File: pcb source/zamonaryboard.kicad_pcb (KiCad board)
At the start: 2 copper layers, 52.3 x 40.6 mm, 19 parts, among them J1 USB_C_Receptacle_USB2.0_14P, SW1 SW_Push, U1 ESP32-S2, U2 ME6211C33M5, Y1 Crystal_GND24

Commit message: Added jlcpcb component annotations, small improvements
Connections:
- U1 pad 30: unconnected-(U1-VDD_SPI-Pad30) -> +3V3
- U1 pad 48: unconnected-(U1-U0TXD/GPIO43-Pad48) -> TX
- U1 pad 49: unconnected-(U1-U0RXD/GPIO44-Pad49) -> RX
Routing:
- net RX: track 0.00 -> 6.73 mm
- net TX: track 0.00 -> 5.18 mm
- net +3V3: track 53.1 -> 57.0 mm, vias 5 -> 6
- net Net-(U1-XTAL_N): track 12.3 -> 13.1 mm
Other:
- board text added: "RX"
- board text added: "TX"
- board text added: "prototype 1.2.1"
- board text removed: "prototype 1.1"

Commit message: big improvements to pcb
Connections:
- C1 pad 1: Net-(C1-Pad1) -> +3V3
- C2 pad 1: Net-(C1-Pad1) -> +3V3
- C3 pad 1: Net-(C1-Pad1) -> +3V3
- U1 pad 3: Net-(C1-Pad1) -> +3V3
- U1 pad 4: Net-(C1-Pad1) -> +3V3
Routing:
- net Net-(C1-Pad1): track 16.4 -> 0.00 mm, vias 2 -> 0
- net +3V3: track 57.0 -> 66.6 mm
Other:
- board text added: "prototype 1.3"
- board text removed: "prototype 1.2.1"

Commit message: exported gerber files for prototype 1.3, cleanup
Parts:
- C8, C9: footprint Capacitor_SMD:C_0805_2012Metric_Pad1.18x1.45mm_HandSolder -> Capacitor_SMD:C_0603_1608Metric_Pad1.08x0.95mm_HandSolder
- Y1: footprint Crystal:Crystal_SMD_3225-4Pin_3.2x2.5mm_HandSoldering -> Crystal:Crystal_SMD_3225-4Pin_3.2x2.5mm
- moved C8 1.04 mm to (153.1, 78.4)
- moved Y1 0.69 mm to (150.3, 78.5)
- moved C9 0.36 mm to (150.3, 75.4)
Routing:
- net GND: track 119.8 -> 105.5 mm
- net Net-(U1-XTAL_N): track 13.1 -> 9.63 mm
- net Net-(U1-XTAL_P): track 6.39 -> 5.77 mm

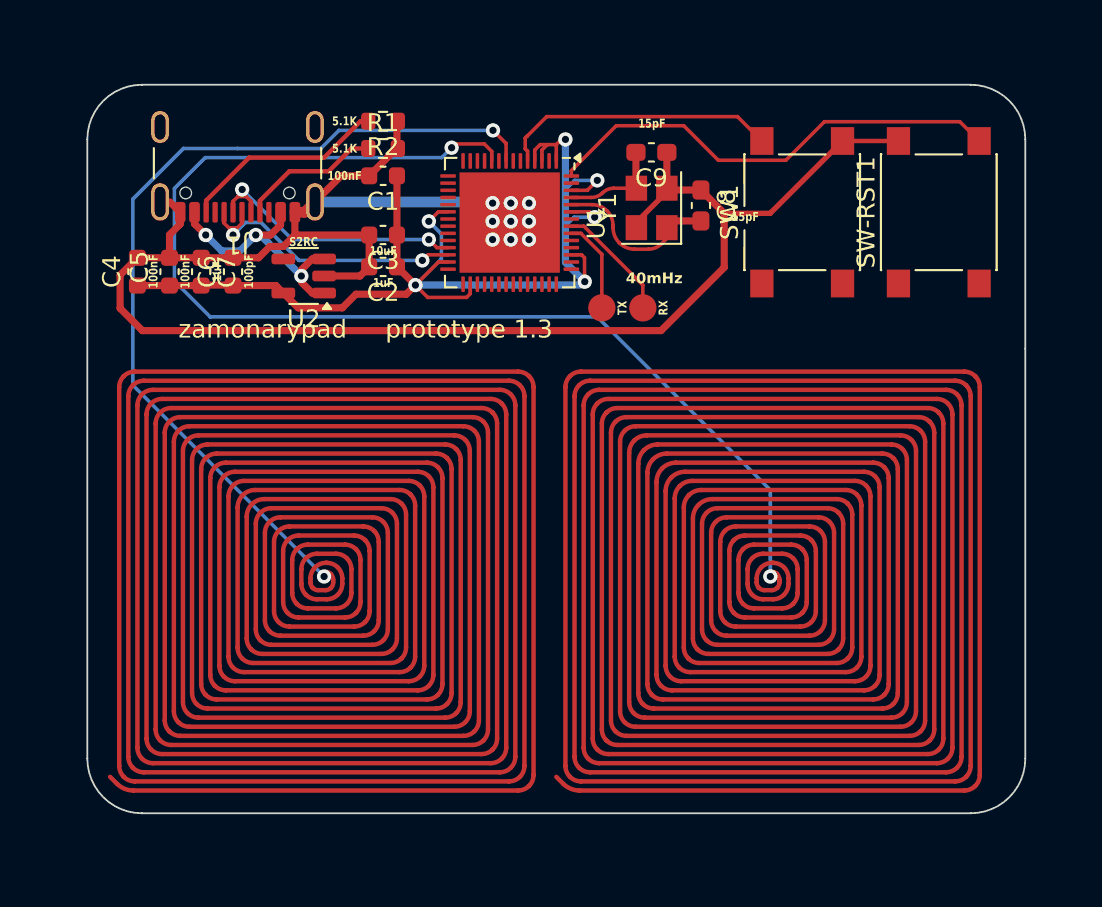
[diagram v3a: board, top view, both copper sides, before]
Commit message: Many improvements to pcb and scheme, added testpoints for easier debugging
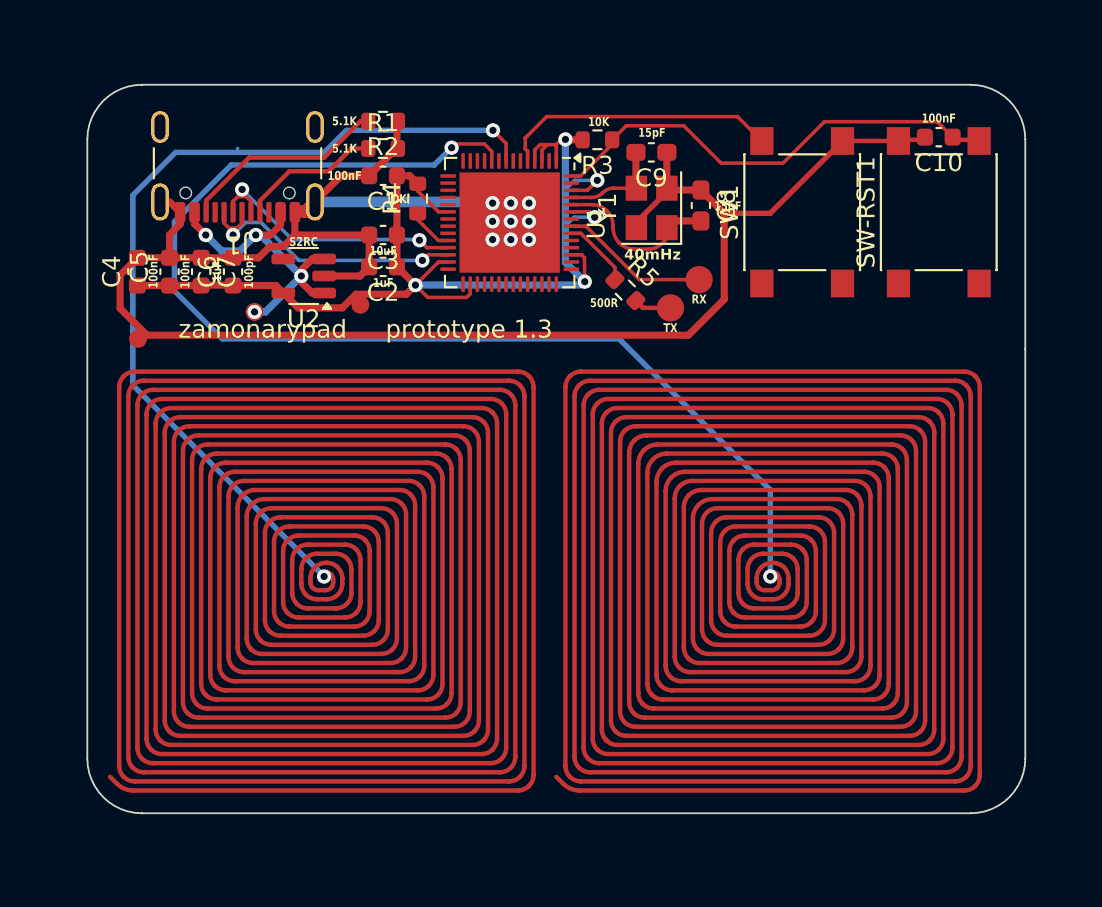
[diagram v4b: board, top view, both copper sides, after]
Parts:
- added C10: 100nF, Capacitor_SMD:C_0603_1608Metric, F.Cu at (166.4, 74.6)
- added R3: 10K, Resistor_SMD:R_0603_1608Metric, F.Cu at (147.3, 74.7)
- added R4: 10K, Resistor_SMD:R_0603_1608Metric, F.Cu at (137.3, 78.0)
- added R5: 500, Resistor_SMD:R_0603_1608Metric, F.Cu at (148.9, 83.1)
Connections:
- U1 pad 24: unconnected-(U1-GPIO18/ADC2_CH7/DAC_2-Pad24) -> Net-(U1-GPIO18/ADC2_CH7/DAC_2)
- U1 pad 48: TX -> Net-(U1-U0TXD/GPIO43)
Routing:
- net Net-(U1-U0TXD/GPIO43): track 0.00 -> 3.90 mm
- net VBUS: track 14.6 -> 18.0 mm, vias 3 -> 4
- net TX: track 5.18 -> 2.10 mm
- net Net-(U1-GPIO18/ADC2_CH7/DAC_2): track 0.00 -> 2.53 mm
- net GND: track 105.5 -> 107.9 mm
- net RX: track 6.62 -> 8.37 mm
- net +3V3: track 66.6 -> 65.6 mm, vias 6 -> 5
- net BTN2: track 1143.1 -> 1142.3 mm
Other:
- board text added: "10K"
- board text added: "500R"

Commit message: improved routing, fixes
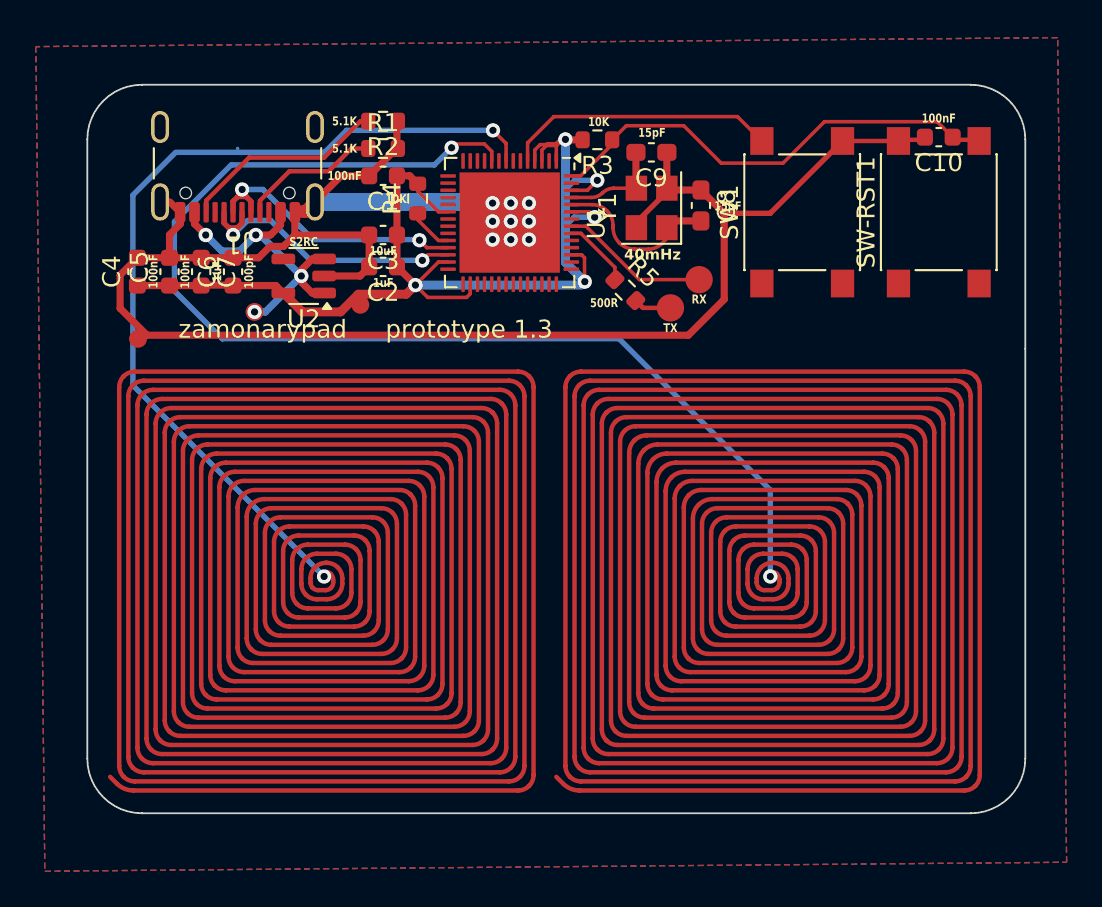
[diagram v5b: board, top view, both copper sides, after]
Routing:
- added copper zone on B.Cu, net (none)
- added copper zone on F.Cu, net (none)
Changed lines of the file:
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@@
 	)
 	(setup
+		(stackup
+			(layer "F.SilkS"
+				(type "Top Silk Screen")
+			)
+			(layer "F.Paste"
+				(type "Top Solder Paste")
+			)
+			(layer "F.Mask"
+				(type "Top Solder Mask")
+				(thickness 0.01)
+			)
+			(layer "F.Cu"
+				(type "copper")
+				(thickness 0.035)
+			)
+			(layer "dielectric 1"
+				(type "core")
+				(thickness 1.51)
+				(material "FR4")
+				(epsilon_r 4.5)
+				(loss_tangent 0.02)
+			)
+			(layer "B.Cu"
+				(type "copper")
+				(thickness 0.035)
+			)
+			(layer "B.Mask"
+				(type "Bottom Solder Mask")
+				(thickness 0.01)
+			)
+			(layer "B.Paste"
+				(type "Bottom Solder Paste")
+			)
+			(layer "B.SilkS"
+				(type "Bottom Silk Screen")
+			)
+			(copper_finish "None")
+			(dielectric_constraints no)
+		)
 		(pad_to_mask_clearance 0)
 		(allow_soldermask_bridges_in_footprints no)
@@
 	)
 	(segment
-		(start 141.411 78.165)
-		(end 141.478 78.232)
-		(width 0.25)
+		(start 142.5 79.25)
+		(end 142.496 79.25)
+		(width 1)
 		(layer "B.Cu")
 		(net 1)
@@
 	(segment
 		(start 131.57 78.165)
-		(end 141.411 78.165)
-		(width 0.6)
+		(end 141.415 78.165)
+		(width 1)
 		(layer "B.Cu")
 		(net 1)
 	)
 	(segment
-		(start 133.858 83.312)
-		(end 136.66464 83.312)
-		(width 0.4)
-		(layer "F.Cu")
-		(net 2)
+		(start 142.496 79.25)
+		(end 142.494 79.248)
+		(width 1)
+		(layer "B.Cu")
+		(net 1)
 	)
 	(segment
@@
 	)
 	(segment
-		(start 133.096 84.074)
-		(end 133.858 83.312)
-		(width 0.4)
+		(start 129.805 83.246)
+		(end 130.859 84.3)
+		(width 0.5)
 		(layer "F.Cu")
 		(net 2)
@@
 		(start 145.032 74.968)
 		(end 144.532 74.968)
-		(width 0.2)
+		(width 0.3)
+		(layer "F.Cu")
+		(net 2)
+	)
+	(segment
+		(start 136.66464 83.312)
+		(end 137.17264 82.804)
+		(width 0.5)
 		(layer "F.Cu")
 		(net 2)
@@
 	)
 	(segment
+		(start 130.859 84.3)
+		(end 133 84.3)
+		(width 0.5)
+		(layer "F.Cu")
+		(net 2)
+	)
+	(segment
 		(start 146.766 77.516)
 		(end 145.8695 77.516)
@@
 	)
 	(segment
-		(start 145.324 74.676)
-		(end 145.032 74.968)
-		(width 0.2)
+		(start 133.988 83.312)
+		(end 136.66464 83.312)
+		(width 0.5)
 		(layer "F.Cu")
 		(net 2)
 	)
 	(segment
-		(start 130.633 84.074)
-		(end 133.096 84.074)
-		(width 0.4)
+		(start 145.324 74.676)
+		(end 145.032 74.968)
+		(width 0.3)
 		(layer "F.Cu")
 		(net 2)
@@
 	)
 	(segment
-		(start 129.805 83.246)
-		(end 130.633 84.074)
-		(width 0.4)
-		(layer "F.Cu")
-		(net 2)
-	)
-	(segment
 		(start 125.248 82.804)
 		(end 125.222 82.83)
@@
 	)
 	(segment
-		(start 136.66464 83.312)
-		(end 137.17264 82.804)
-		(width 0.4)
-		(layer "F.Cu")
-		(net 2)
-	)
-	(segment
 		(start 144.232 75.268)
 		(end 144.232 75.8785)
@@
 	)
 	(segment
+		(start 133 84.3)
+		(end 133.988 83.312)
+		(width 0.5)
+		(layer "F.Cu")
+		(net 2)
+	)
+	(segment
 		(start 129.389 82.83)
 		(end 129.805 83.246)
@@
 		(start 147.174275 79.016)
 		(end 146.028 79.016)
-		(width 0.2)
+		(width 0.3)
 		(layer "B.Cu")
 		(net 2)
@@
 		(start 146.05 76.962)
 		(end 145.542 77.47)
-		(width 0.2)
+		(width 0.3)
 		(layer "B.Cu")
 		(net 2)
@@
 		(start 146.431 82.804)
 		(end 137.17264 82.804)
-		(width 0.4)
+		(width 0.5)
 		(layer "B.Cu")
 		(net 2)
@@
 		(start 147.32 76.962)
 		(end 146.05 76.962)
-		(width 0.2)
+		(width 0.3)
 		(layer "B.Cu")
 		(net 2)
@@
 		(start 146.6215 82.6135)
 		(end 145.542 81.534)
-		(width 0.4)
+		(width 0.5)
 		(layer "B.Cu")
 		(net 2)
@@
 		(start 145.542 81.534)
 		(end 145.542 79.756)
-		(width 0.4)
+		(width 0.5)
 		(layer "B.Cu")
 		(net 2)
@@
 		(start 145.542 79.756)
 		(end 145.542 77.47)
-		(width 0.4)
+		(width 0.5)
 		(layer "B.Cu")
 		(net 2)
@@
 		(start 145.542 74.676)
 		(end 145.542 77.47)
-		(width 0.4)
+		(width 0.5)
 		(layer "B.Cu")
 		(net 2)
@@
 		(start 146.028 79.016)
 		(end 145.542 79.502)
-		(width 0.2)
+		(width 0.3)
 		(layer "B.Cu")
 		(net 2)
@@
 		(start 126.5 79.34741)
 		(end 126.5 78.74)
-		(width 0.2)
+		(width 0.3)
 		(layer "F.Cu")
 		(net 3)
@@
 		(start 127.23241 79.615)
 		(end 126.76759 79.615)
-		(width 0.2)
+		(width 0.3)
 		(layer "F.Cu")
 		(net 3)
@@
 		(start 126.76759 79.615)
 		(end 126.5 79.34741)
-		(width 0.2)
+		(width 0.3)
 		(layer "F.Cu")
 		(net 3)
@@
 		(start 127.5 79.34741)
 		(end 127.23241 79.615)
-		(width 0.2)
+		(width 0.3)
 		(layer "F.Cu")
 		(net 3)
@@
 		(start 127.5 78.74)
 		(end 127.5 79.34741)
-		(width 0.2)
+		(width 0.3)
 		(layer "F.Cu")
 		(net 3)
@@
 	)
 	(segment
-		(start 127.7 79.31)
-		(end 127 80.01)
-		(width 0.2)
+		(start 129.1 79.2)
+		(end 127.81 79.2)
+		(width 0.3)
 		(layer "B.Cu")
 		(net 3)
 	)
 	(segment
-		(start 137.560345 81.426345)
-		(end 130.676295 81.426345)
-		(width 0.2)
+		(start 131.326345 81.426345)
+		(end 129.1 79.2)
+		(width 0.3)
 		(layer "B.Cu")
 		(net 3)
 	)
 	(segment
-		(start 128.55995 79.31)
-		(end 127.7 79.31)
-		(width 0.2)
+		(start 127.81 79.2)
+		(end 127 80.01)
+		(width 0.3)
 		(layer "B.Cu")
 		(net 3)
 	)
 	(segment
-		(start 130.676295 81.426345)
-		(end 128.55995 79.31)
-		(width 0.2)
+		(start 137.560345 81.426345)
+		(end 131.326345 81.426345)
+		(width 0.3)
 		(layer "B.Cu")
 		(net 3)
@@
 		(start 128 78.13259)
 		(end 128 78.74)
-		(width 0.2)
+		(width 0.3)
 		(layer "F.Cu")
 		(net 6)
@@
 		(start 127.26759 77.865)
 		(end 127.73241 77.865)
-		(width 0.2)
+		(width 0.3)
 		(layer "F.Cu")
 		(net 6)
@@
 		(start 127 78.74)
 		(end 127 78.13259)
-		(width 0.2)
+		(width 0.3)
 		(layer "F.Cu")
 		(net 6)
@@
 		(start 127.73241 77.865)
 		(end 128 78.13259)
-		(width 0.2)
+		(width 0.3)
 		(layer "F.Cu")
 		(net 6)
@@
 		(start 127 78.13259)
 		(end 127.26759 77.865)
-		(width 0.2)
+		(width 0.3)
 		(layer "F.Cu")
 		(net 6)
@@
 	)
 	(segment
-		(start 137.4 80.3)
-		(end 137.364 80.264)
-		(width 0.2)
+		(start 137.364 80.264)
+		(end 131.464 80.264)
+		(width 0.3)
 		(layer "B.Cu")
 		(net 6)
 	)
 	(segment
-		(start 137.364 80.264)
-		(end 130.302 80.264)
-		(width 0.2)
+		(start 128.67 77.47)
+		(end 127.508 77.47)
+		(width 0.3)
 		(layer "B.Cu")
 		(net 6)
 	)
 	(segment
-		(start 130.302 80.264)
-		(end 127.508 77.47)
+		(start 137.4 80.3)
+		(end 137.364 80.264)
 		(width 0.2)
 		(layer "B.Cu")
@@
 	)
 	(segment
+		(start 131.464 80.264)
+		(end 128.67 77.47)
+		(width 0.3)
+		(layer "B.Cu")
+		(net 6)
+	)
+	(segment
 		(start 134.594 75.184)
 		(end 133.604 75.184)
@@
 	)
 	(segment
-		(start 155.141 73.406)
-		(end 144.496877 73.406)
-		(width 0.2)
-		(layer "F.Cu")
-		(net 9)
-	)
-	(segment
-		(start 143.432 75.332)
-		(end 143.432 75.8785)
-		(width 0.2)
-		(layer "F.Cu")
-		(net 9)
-	)
-	(segment
-		(start 143.402877 74.5)
-		(end 143.4 74.5)
-		(width 0.2)
-		(layer "F.Cu")
-		(net 9)
-	)
-	(segment
 		(start 156.5 74.765)
 		(end 155.141 73.406)
@@
 	)
 	(segment
-		(start 143.4 74.5)
-		(end 143.3 74.6)
-		(width 0.2)
-		(layer "F.Cu")
-		(net 9)
-	)
-	(segment
-		(start 143.3 75.2)
-		(end 143.432 75.332)
+		(start 155.141 73.406)
+		(end 144.894 73.406)
 		(width 0.2)
 		(layer "F.Cu")
@@
 	)
 	(segment
-		(start 143.3 74.6)
-		(end 143.3 75.2)
+		(start 143.432 74.868)
+		(end 143.432 75.8785)
 		(width 0.2)
 		(layer "F.Cu")
@@
 	)
 	(segment
-		(start 144.496877 73.406)
-		(end 143.402877 74.5)
+		(start 144.894 73.406)
+		(end 143.432 74.868)
 		(width 0.2)
 		(layer "F.Cu")
@@
 		(net 54)
 	)
+	(zone
+		(net 0)
+		(net_name "")
+		(layers "F&B.Cu")
+		(hatch edge 0.5)
+		(priority 1)
+		(connect_pads
+			(clearance 0.4)
+		)
+		(min_thickness 0.25)
+		(filled_areas_thickness no)
+		(fill
+			(thermal_gap 0.8)
+			(thermal_bridge_width 0.3)
+			(island_removal_mode 1)
+			(island_area_min 10)
+		)
+		(polygon
+			(pts
+				(xy 116 69.5) (xy 116.5 115.5) (xy 173.5 115) (xy 173 69)
+			)
+		)
+	)
 	(group ""

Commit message: Improvements on pcb, more components, better routing and better labling.
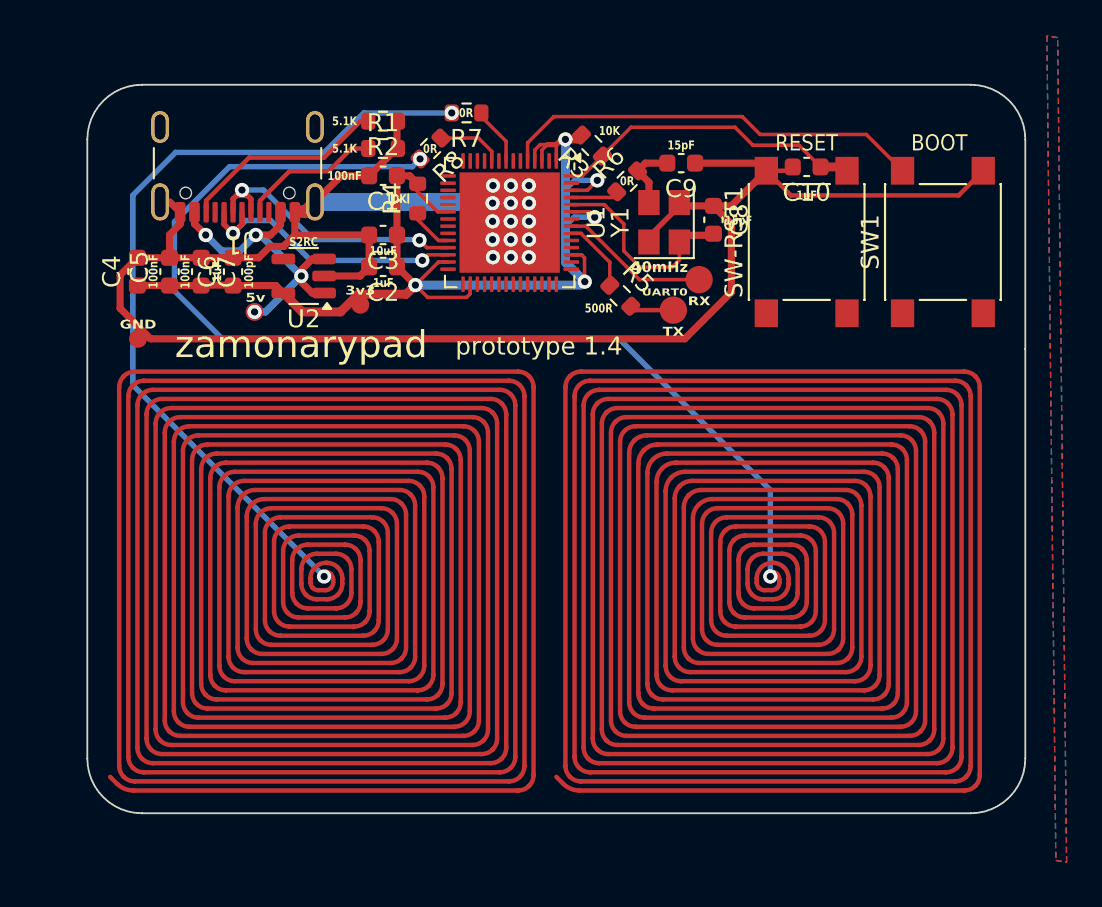
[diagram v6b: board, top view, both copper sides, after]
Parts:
- added R6: 0, Resistor_SMD:R_0603_1608Metric, F.Cu at (149.0, 77.0)
- added R7: 0, Resistor_SMD:R_0603_1608Metric, F.Cu at (140.0, 73.2)
- added R8: 0, Resistor_SMD:R_0603_1608Metric, F.Cu at (138.0, 75.2)
- C10: value 100nF -> 1uF
- C8, C9: footprint Capacitor_SMD:C_0603_1608Metric_Pad1.08x0.95mm_HandSolder -> Capacitor_SMD:C_0603_1608Metric
- moved SW1 8.02 mm to (166.6, 80.4)
- moved SW-RST1 7.55 mm to (159.0, 80.4)
- moved C10 7.55 mm to (159.0, 76.2)
- moved C9 1.77 mm to (152.0, 76.0)
- moved C8 1.06 mm to (153.8, 79.2)
- moved Y1 1.06 mm to (151.1, 79.3)
- moved R3 0.44 mm to (147.0, 75.0), turned to 135 degrees
- moved R5 0.42 mm to (148.6, 83.4)
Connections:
- C9 pad 2: Net-(U1-XTAL_P) -> Net-(C9-Pad2)
- U1 pad 10: BTN2 -> Net-(U1-GPIO5/ADC1_CH4)
- U1 pad 8: BTN1 -> Net-(U1-GPIO3/ADC1_CH2)
- Y1 pad 3: Net-(U1-XTAL_P) -> Net-(C9-Pad2)
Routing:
- net Net-(U1-CHIP_PU/RESET): track 26.2 -> 17.5 mm
- net Net-(U1-GPIO0/BOOT): track 15.2 -> 23.8 mm
- net GND: track 107.8 -> 113.2 mm, vias 9 -> 15
- net BTN2: track 1142.3 -> 1137.3 mm
- net BTN1: track 1125.4 -> 1121.5 mm
- net Net-(C9-Pad2): track 0.00 -> 3.87 mm
- net Net-(U1-GPIO5/ADC1_CH4): track 0.00 -> 3.67 mm
- net Net-(U1-XTAL_P): track 5.77 -> 2.61 mm
- net Net-(U1-GPIO3/ADC1_CH2): track 0.00 -> 3.05 mm
- net Net-(U1-XTAL_N): track 9.63 -> 11.0 mm
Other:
- board text added: "0R"
- board text added: "3v3"
- board text added: "5v"
- board text added: "BOOT"
- board text added: "GND"
- board text added: "RESET"
- board text added: "UART0"
- board text added: "prototype 1.4"
- board text removed: "prototype 1.3"
